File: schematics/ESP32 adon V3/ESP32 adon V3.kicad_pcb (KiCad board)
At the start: 2 copper layers, 42 x 64.1 mm, 43 parts, among them J1 Conn_01x08_Pin, J10 Conn_01x01, J11 Conn_01x01, J12 Conn_01x01, J13 Conn_01x01, J14 Conn_01x01, J2 Conn_01x08_Pin, J3 Conn_01x02_Pin, J4 Conn_01x08_Pin, J5 Conn_01x08_Pin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

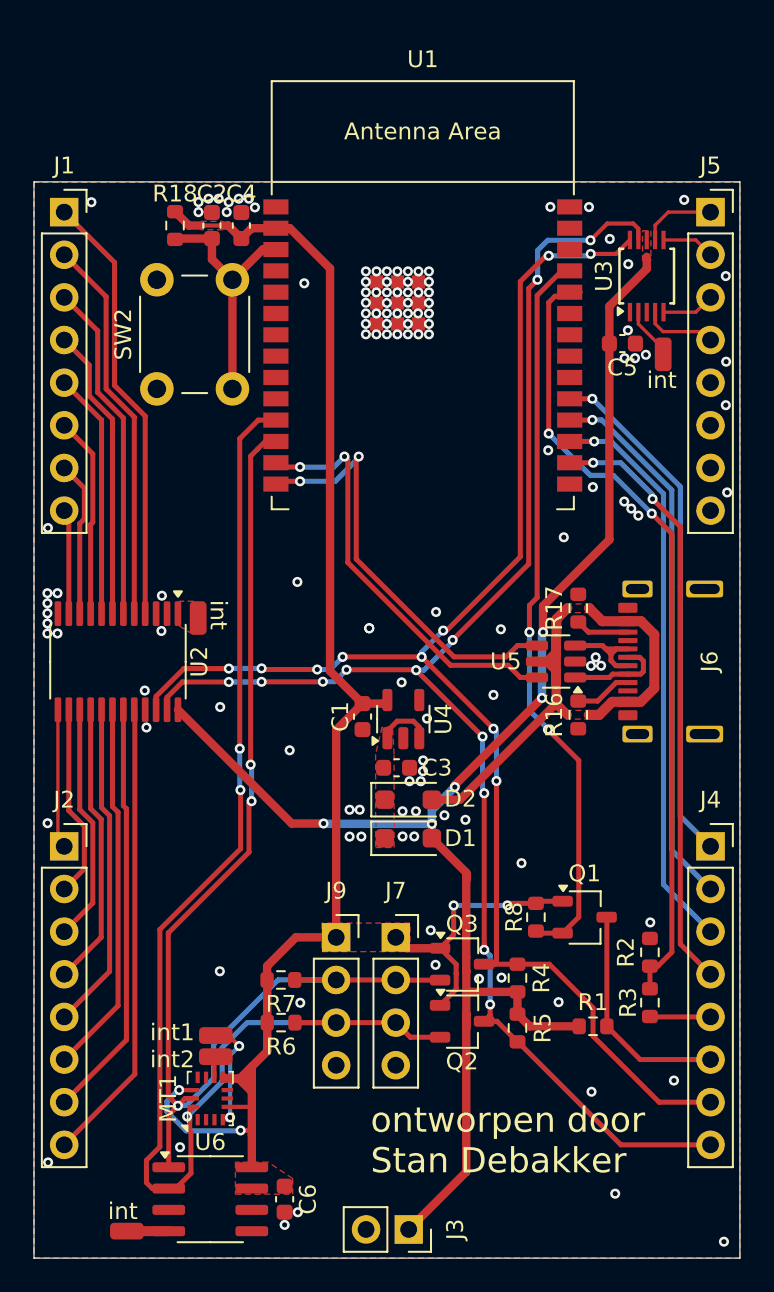
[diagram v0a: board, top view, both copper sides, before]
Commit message: update de .gitignore en voeg viea's toe aan ESP32 addon V3
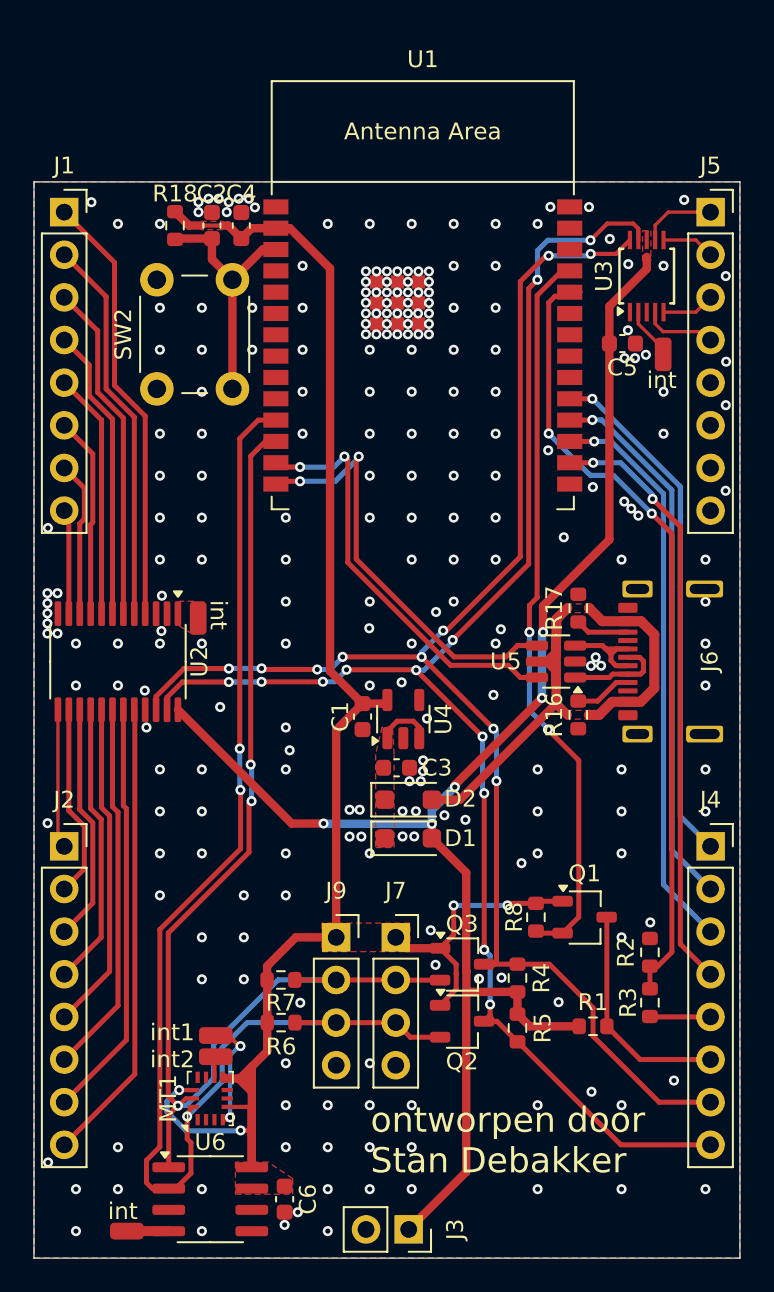
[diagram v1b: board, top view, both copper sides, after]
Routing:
- net +3.3V: track 102.3 -> 105.8 mm
- net +5V: track 93.5 -> 91.8 mm
- net GND: vias 127 -> 249

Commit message: pas de maten aan van de addon V3 en de lijnsensor(nog niet klaar)
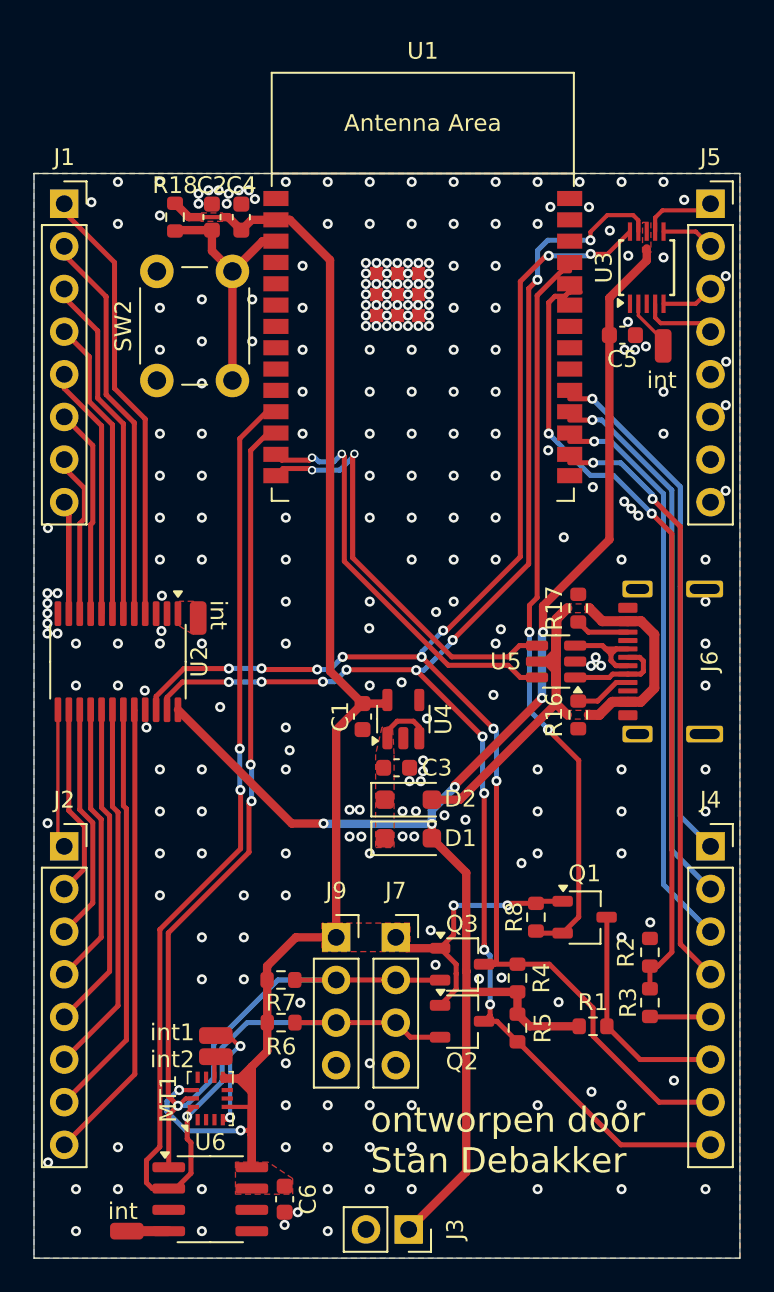
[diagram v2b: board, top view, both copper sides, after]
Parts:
- moved C2 0.50 mm to (60.6, 32.1)
- moved C4 0.50 mm to (62.4, 32.1)
- moved C5 0.50 mm to (85.0, 39.1)
- moved J1 0.50 mm to (51.8, 31.3)
- moved J11 0.50 mm to (87.5, 39.8)
- moved J5 0.50 mm to (90.3, 31.3)
- moved R18 0.50 mm to (58.4, 32.1)
- moved SW2 0.50 mm to (57.3, 41.8)
- moved U1 0.50 mm to (73.2, 39.2)
- moved U3 0.50 mm to (86.5, 35.1)
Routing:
- net Net-(J1-Pin_8): track 6.25 -> 13.0 mm
- net /D+: track 25.8 -> 31.6 mm
- net Net-(J1-Pin_5): track 14.7 -> 15.2 mm
- net Net-(J1-Pin_6): track 12.0 -> 12.5 mm
- net Net-(J1-Pin_4): track 17.5 -> 18.0 mm
- net +3.3V: track 105.8 -> 106.3 mm
- net GND: vias 249 -> 248
- net (no net): vias 0 -> 12
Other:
- board size 42 x 64.1 mm -> 42 x 64.6 mm

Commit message: maak de .gbr bestanden
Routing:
- net Net-(U1-U0RXD/GPIO17): track 47.7 -> 48.4 mm
- net Net-(J4-Pin_4): track 35.7 -> 36.3 mm
- net Net-(J4-Pin_1): track 30.9 -> 31.5 mm
- net Net-(J4-Pin_3): track 34.1 -> 34.7 mm
- net Net-(J4-Pin_2): track 32.5 -> 33.1 mm
- net /SCL_{5V}: track 89.0 -> 89.5 mm
- net Net-(Q1-S): track 44.0 -> 44.5 mm
- net GND: vias 248 -> 262
- net (no net): vias 12 -> 0
